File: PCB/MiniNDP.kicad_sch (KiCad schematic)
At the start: 20 parts, among them J1 Conn_02x20_Odd_Even, U1 HC161, U2 HC161, U3 HC161, U4 HC138, U5 HC574, U6 AS6C4008, U7 1G32, U8 1G79

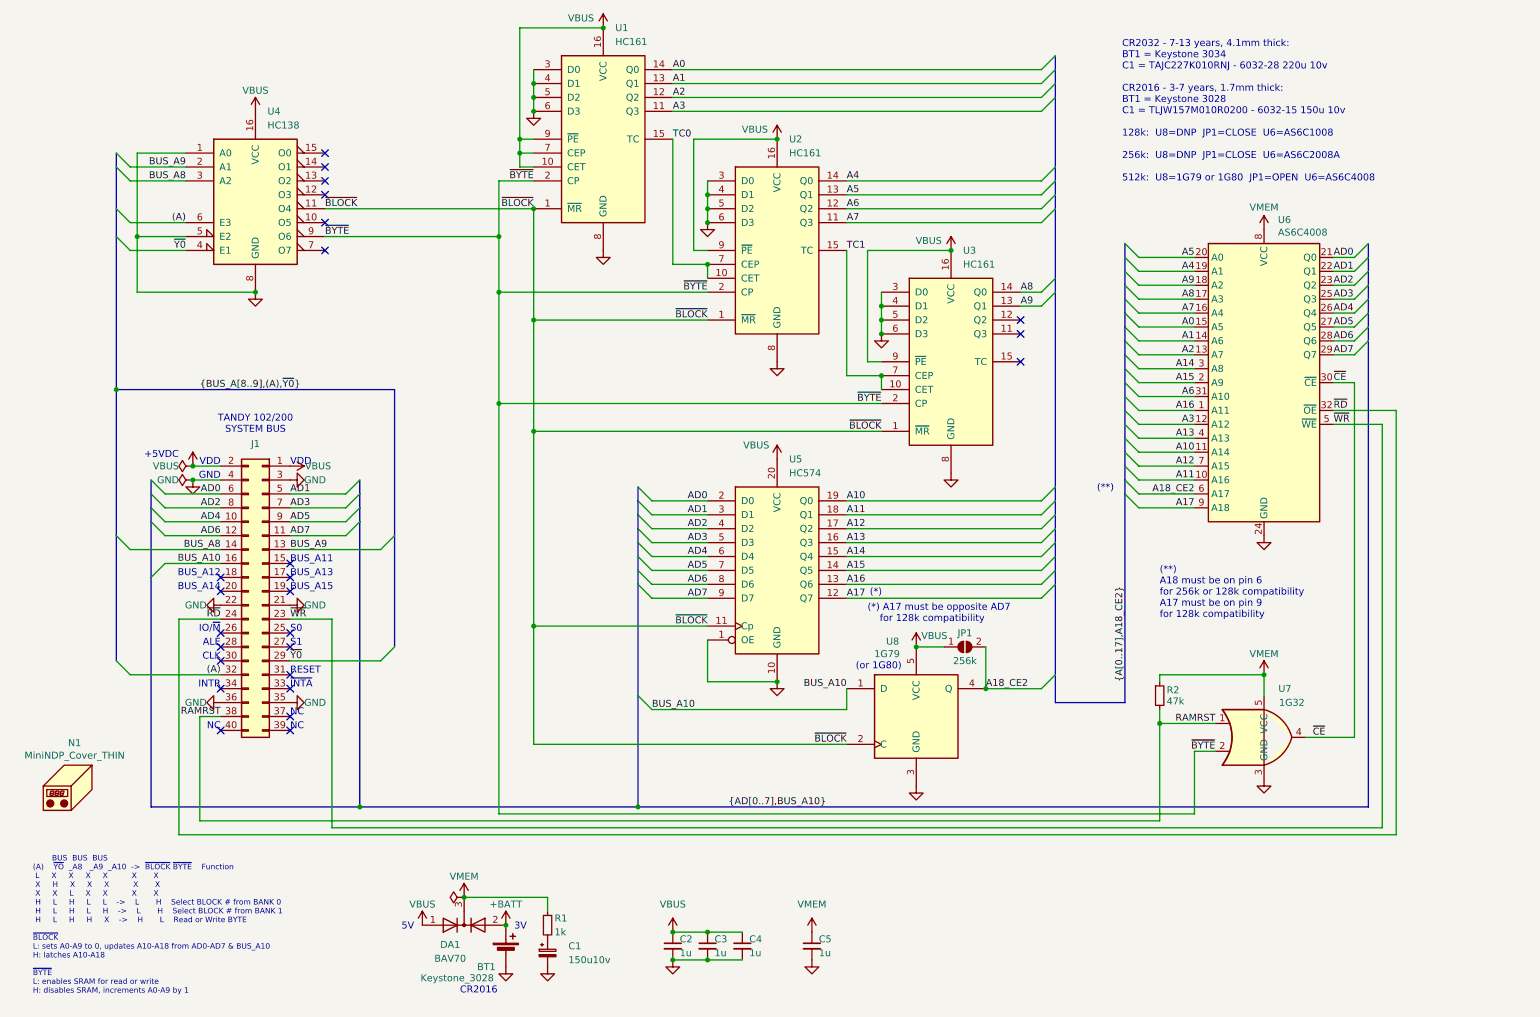
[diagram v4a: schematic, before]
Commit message: make EZ1M the default
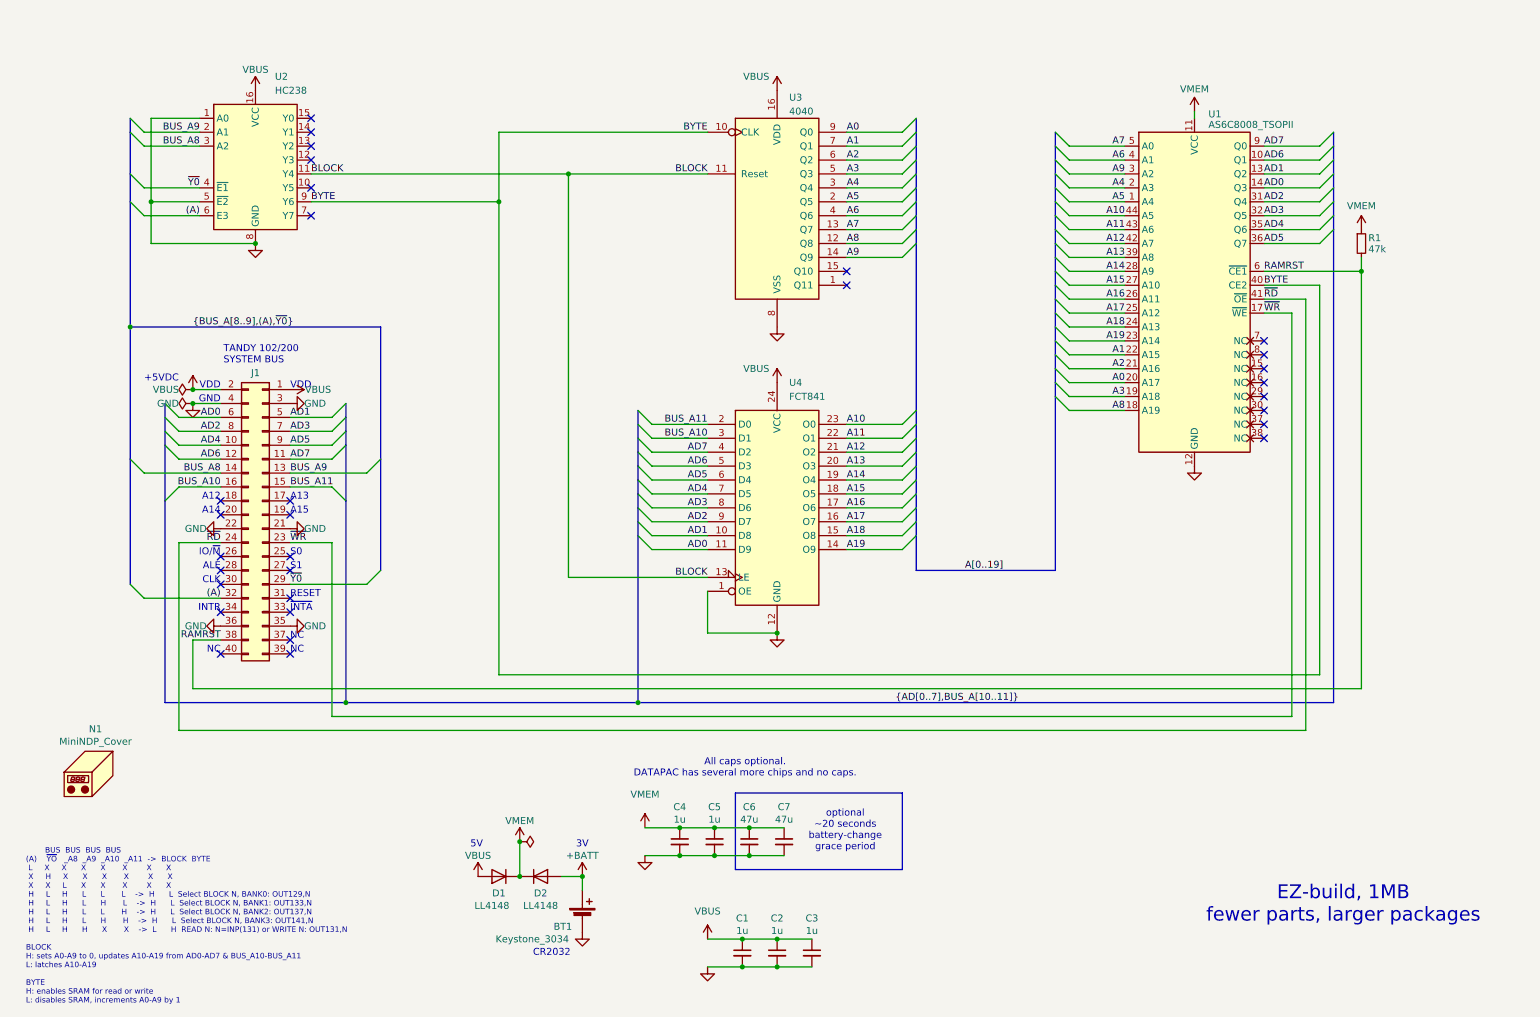
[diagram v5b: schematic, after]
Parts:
- removed C1: 150u10v, 000_LOCAL:CP_6032, symbol 000_LOCAL:C_Polarized
- removed DA1: BAV70, 000_LOCAL:SOT-23, symbol 000_LOCAL:BAV70
- removed JP1: 256k, 000_LOCAL:SolderJumper-2_Open 0.65mm, symbol 000_LOCAL:SolderJumper_2_Open
- removed R1: 1k, 000_LOCAL:R_0805, symbol 000_LOCAL:R
- removed U1, U2, U3: HC161, 000_LOCAL:TSSOP-16, symbol 000_LOCAL:74xx161
- removed U4: HC138, 000_LOCAL:TSSOP-16, symbol 000_LOCAL:74xx138
- removed U5: HC574, 000_LOCAL:TSSOP-20, symbol 000_LOCAL:74xx574
- removed U7: 1G32, 000_LOCAL:SOT-353_SC-70-5, symbol 000_LOCAL:74xx1G32
- removed U8: 1G79, 000_LOCAL:SOT-353_SC-70-5, symbol 000_LOCAL:74xx1G79
- added C1: 1u, 000_LOCAL:C_0805, symbol 000_LOCAL:C
- added C6, C7: 47u, 000_LOCAL:C_1206, symbol 000_LOCAL:C
- added D1, D2: LL4148, 000_LOCAL:D_MiniMELF, symbol 000_LOCAL:LL4148
- added U2: HC238, 000_LOCAL:SOIC-16_3.9x9.9mm_P1.27mm, symbol 000_LOCAL:HC238
- added U3: 4040, 000_LOCAL:SOIC-16_3.9x9.9mm_P1.27mm, symbol 000_LOCAL:4040
- added U4: FCT841, 000_LOCAL:SOIC-24, symbol 000_LOCAL:FCT841
- BT1: value Keystone_3028 -> Keystone_3034; MPN Keystone_3028 -> Keystone 3034
- N1: value MiniNDP_Cover_THIN -> MiniNDP_Cover; footprint 000_LOCAL:MiniNDP_Cover_THIN -> 000_LOCAL:MiniNDP_Cover; MPN MiniNDP_Cover_THIN.stl -> MiniNDP_Cover.stl
- U1: renamed from U6; value AS6C4008 -> AS6C8008_TSOPII; footprint 000_LOCAL:TSOP32-dual -> 000_LOCAL:TSOP-II-44; symbol 000_LOCAL:AS6C4008_TSOP -> 000_LOCAL:AS6C8008_TSOPII; MPN AS6C4008-55STIN -> AS6C8008-55ZIN
- renumbered R2 to R1
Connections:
- net A18_CE2 is gone; now on net RAMRST: U1.6 (~{CE1})
- net (A): now also U2.6 (E3)
- net +BATT: now also D2.2 (A)
- net A0: now also U1.20 (A17), U3.9 (Q0); no longer U1.15 (A5)
- net A1: now also U1.22 (A15), U3.7 (Q1); no longer U1.14 (A6)
- net A10: now also U1.44 (A5), U4.23 (O0); no longer U1.11 (A14)
- net A11: now also U1.43 (A6), U4.22 (O1); no longer U1.10 (A16)
- net A12: now also U1.42 (A7), U4.21 (O2); no longer U1.7 (A15)
- net A13: now also U1.39 (A8), U4.20 (O3); no longer U1.4 (A13)
- net A14: now also U1.28 (A9), U4.19 (O4); no longer U1.3 (A8)
- net A15: now also U1.27 (A10), U4.18 (O5); no longer U1.2 (A9)
- net A16: now also U1.26 (A11), U4.17 (O6); no longer U1.1 (A11)
- net A17: now also U1.25 (A12), U4.16 (O7); no longer U1.9 (A18)
- net A2: now also U1.21 (A16), U3.6 (Q2); no longer U1.13 (A7)
- net A3: now also U1.19 (A18), U3.5 (Q3); no longer U1.12 (A12)
- net A4: now also U1.2 (A3), U3.3 (Q4); no longer U1.19 (A1)
- net A5: now also U1.1 (A4), U3.2 (Q5); no longer U1.20 (A0)
- net A6: now also U1.4 (A1), U3.4 (Q6); no longer U1.31 (A10)
- net A7: now also U1.5 (A0), U3.13 (Q7); no longer U1.16 (A4)
- net A8: now also U1.18 (A19), U3.12 (Q8); no longer U1.17 (A3)
- net A9: now also U1.3 (A2), U3.14 (Q9); no longer U1.18 (A2)
- net AD0: now also U1.14 (Q3), U4.11 (D9); no longer U1.21 (Q0)
- net AD1: now also U1.13 (Q2), U4.10 (D8); no longer U1.22 (Q1)
- net AD2: now also U1.31 (Q4), U4.9 (D7); no longer U1.23 (Q2)
- net AD3: now also U1.32 (Q5), U4.8 (D6); no longer U1.25 (Q3)
- net AD4: now also U1.35 (Q6), U4.7 (D5); no longer U1.26 (Q4)
- net AD5: now also U1.36 (Q7), U4.6 (D4); no longer U1.27 (Q5)
- net AD6: now also U1.10 (Q1), U4.5 (D3); no longer U1.28 (Q6)
- net AD7: now also U1.9 (Q0), U4.4 (D2); no longer U1.29 (Q7)
- net BUS_A10: now also U4.3 (D1)
- net BUS_A8: now also U2.3 (A2)
- net BUS_A9: now also U2.2 (A1)
- net GND: now also U1.12 (GND), U1.34 (GND), C1.2, C6.2, C7.2, U2.1 (A0), U2.5 (~{E2}), U2.8 (GND), U3.8 (VSS), U4.1 (OE), U4.12 (GND); no longer U1.24 (GND)
- net VBUS: now also C1.1, D1.2 (A), U2.16 (VCC), U3.16 (VDD), U4.24 (VCC); no longer C4.1
- net VMEM: now also C4.1, U1.11 (VCC), U1.33 (VCC), C6.1, C7.1, D1.1 (K), D2.1 (K); no longer U1.8 (VCC)
- net ~{RD}: now also U1.41 (~{OE}); no longer U1.32 (~{OE})
- net ~{WR}: now also U1.17 (~{WE}); no longer U1.5 (~{WE})
- net ~{Y0}: now also U2.4 (~{E1})
- net BUS_A11: now reaches J1.15 (Pin_15)
- net BUS_A11: now also U4.2 (D0)
- net ~{CE}: no longer names the net of U1.30 (NC)
- new net A18: U1.24 (A13), U4.15 (O8)
- new net A19: U1.23 (A14), U4.14 (O9)
- new net BLOCK: U2.11 (Y4), U3.11 (Reset), U4.13 (LE)
- new net BYTE: U1.40 (CE2), U2.9 (Y6), U3.10 (CLK)
- no-connect marks 25 -> 31
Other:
- note added: "A12"
- note added: "A13"
- note added: "A14"
- note added: "A15"
- note added: "All caps optional. DATAPAC has several more chips and no caps."
- note added: "BUS BUS BUS BUS (A) ~{YO} _A8 _A9 _A10 _A11 -> BLOCK BYTE L X X X X X X X X H X X X X X X X X L X X X X X H L H L L L -> H L Select BLOCK N, BANK0: OUT129,N H L H L H L -> H L Select BLOCK N, BANK1: OUT133,N H L H L L H -> H L Select BLOCK N, BANK2: OUT137,N H L H L H H -> H L Select BLOCK N, BANK3: OUT141,N H L H H X X -> L H READ N: N=INP(131) or WRITE N: OUT131,N BLOCK H: sets A0-A9 to 0, upda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"
- note added: "CR2032"
- note added: "EZ-build, 1MB fewer parts, larger packages"
- note added: "optional ~20 seconds battery-change grace period"
- note removed: "(*)"
- note removed: "(*) A17 must be opposite AD7 for 128k compatibility"
- note removed: "(**)"
- note removed: "(**) A18 must be on pin 6 for 256k or 128k compatibility A17 must be on pin 9 for 128k compatibility"
- note removed: "(or 1G80)"
- note removed: "BUS BUS BUS (A) ~{YO} _A8 _A9 _A10 -> ~{BLOCK} ~{BYTE} Function L X X X X X X X H X X X X X X X L X X X X H L H L L -> L H Select BLOCK # from BANK 0 H L H L H -> L H Select BLOCK # from BANK 1 H L H H X -> H L Read or Write BYTE ~{BLOCK} L: sets A0-A9 to 0, updates A10-A18 from AD0-AD7 & BUS_A10 H: latches A10-A18 ~{BYTE} L: enables SRAM for read or write H: disables SRAM, increments A0-A9 by 1"
- note removed: "BUS_A11"
- note removed: "BUS_A12"
- note removed: "BUS_A13"
- note removed: "BUS_A14"
- note removed: "BUS_A15"
- note removed: "CR2016"
- note removed: "CR2032 - 7-13 years, 4.1mm thick: BT1 = Keystone 3034 C1 = TAJC227K010RNJ - 6032-28 220u 10v CR2016 - 3-7 years, 1.7mm thick: BT1 = Keystone 3028 C1 = TLJW157M010R0200 - 6032-15 150u 10v 128k: U8=DNP JP1=CLOSE U6=AS6C1008 256k: U8=DNP JP1=CLOSE U6=AS6C2008A 512k: U8=1G79 or 1G80 JP1=OPEN U6=AS6C4008"
- moved on the sheet: BT1, J1, R1

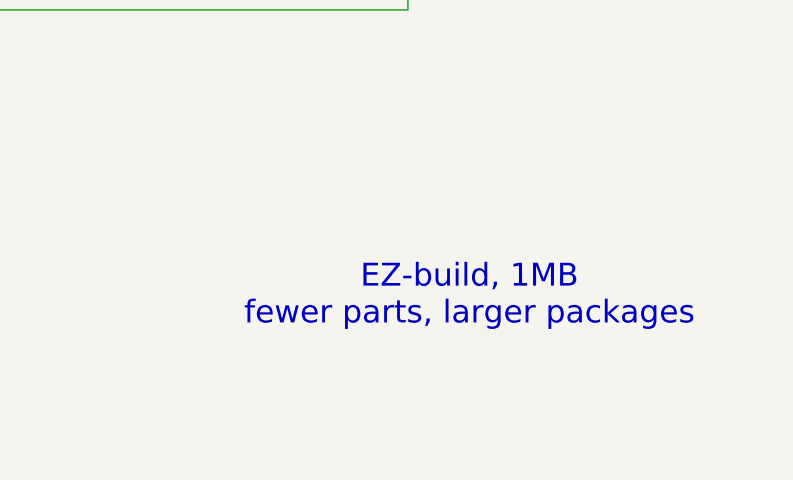
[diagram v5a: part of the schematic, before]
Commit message: ez1m rear silkscreen programming reference
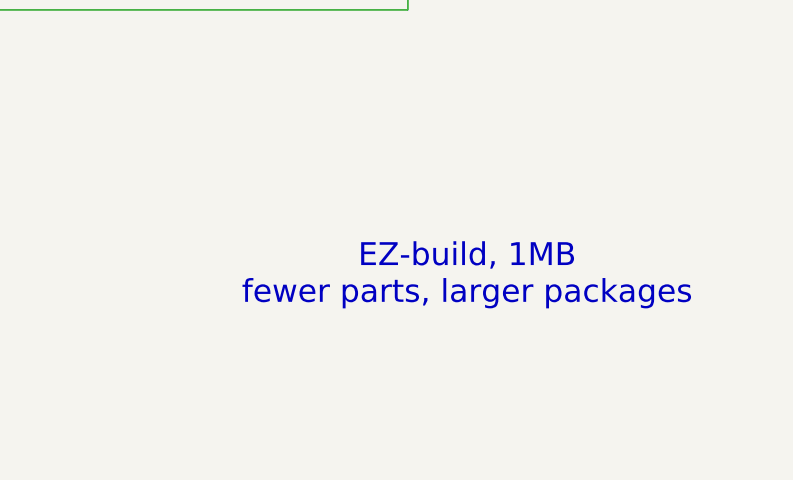
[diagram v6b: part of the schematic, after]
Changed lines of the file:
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@@
 	(text "EZ-build, 1MB\nfewer parts, larger packages"
 		(exclude_from_sim no)
-		(at 255.778 176.53 0)
+		(at 255.524 174.244 0)
 		(effects
 			(font

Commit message: silkscreen & pics
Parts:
- U3: value 4040 -> HC4040
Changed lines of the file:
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@@
 			)
 		)
-		(property "Value" "4040"
+		(property "Value" "HC4040"
 			(at 154.5941 31.75 0)
 			(effects

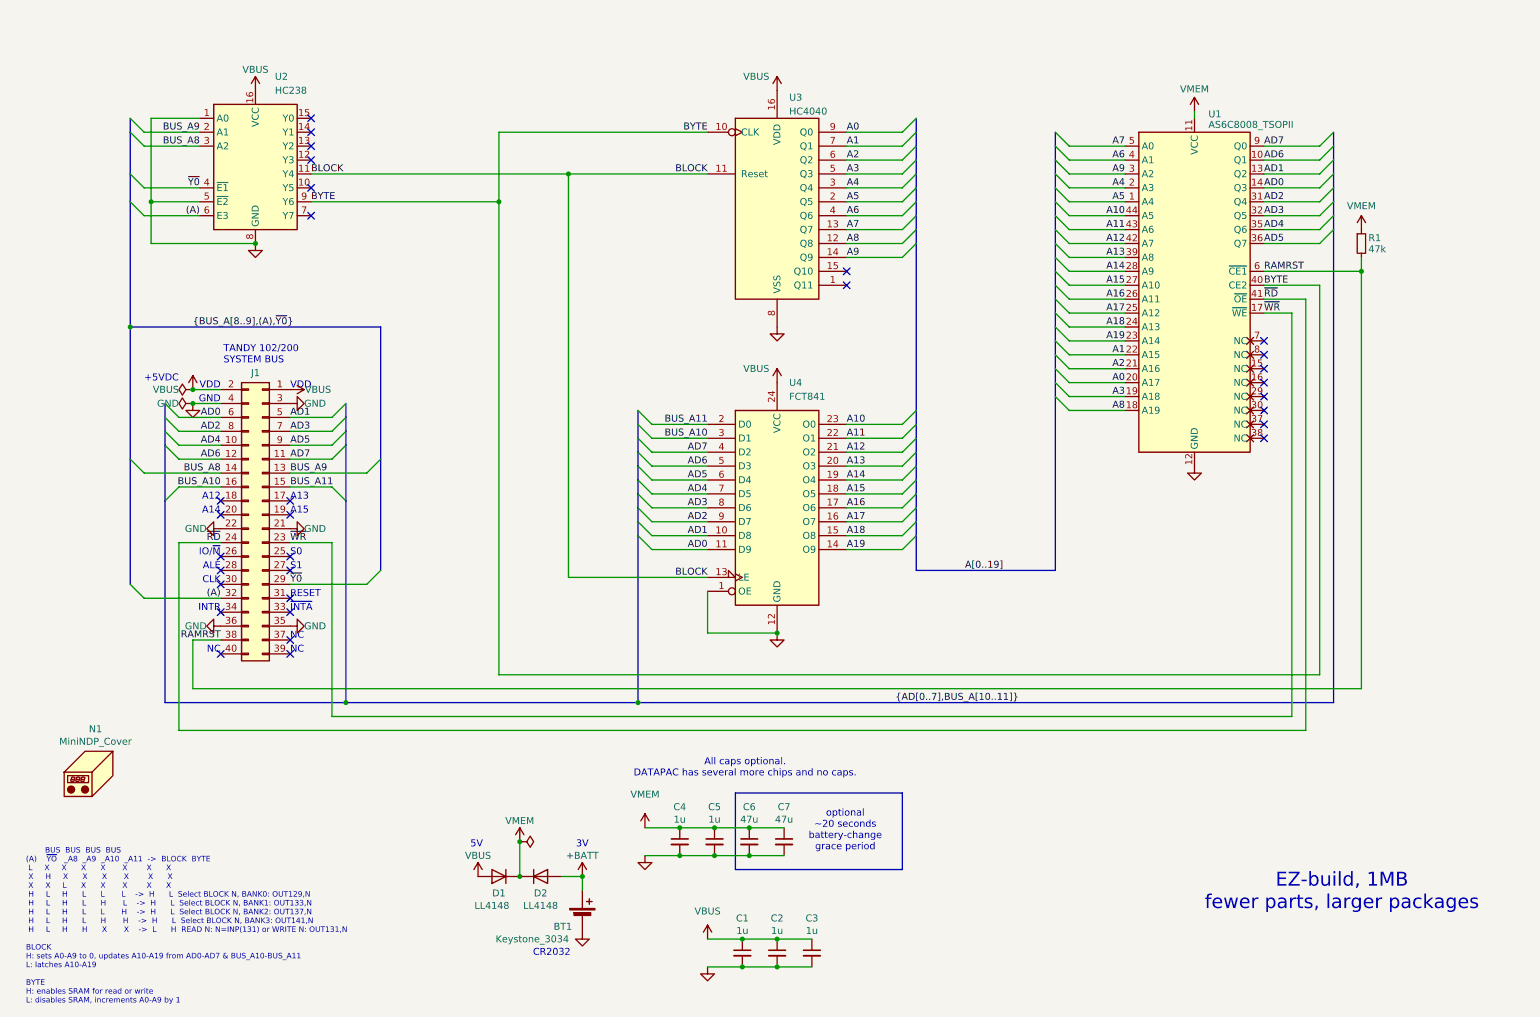
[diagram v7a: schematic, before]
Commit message: embed code font in pcb, bom export filename variables, delete extra battery trace
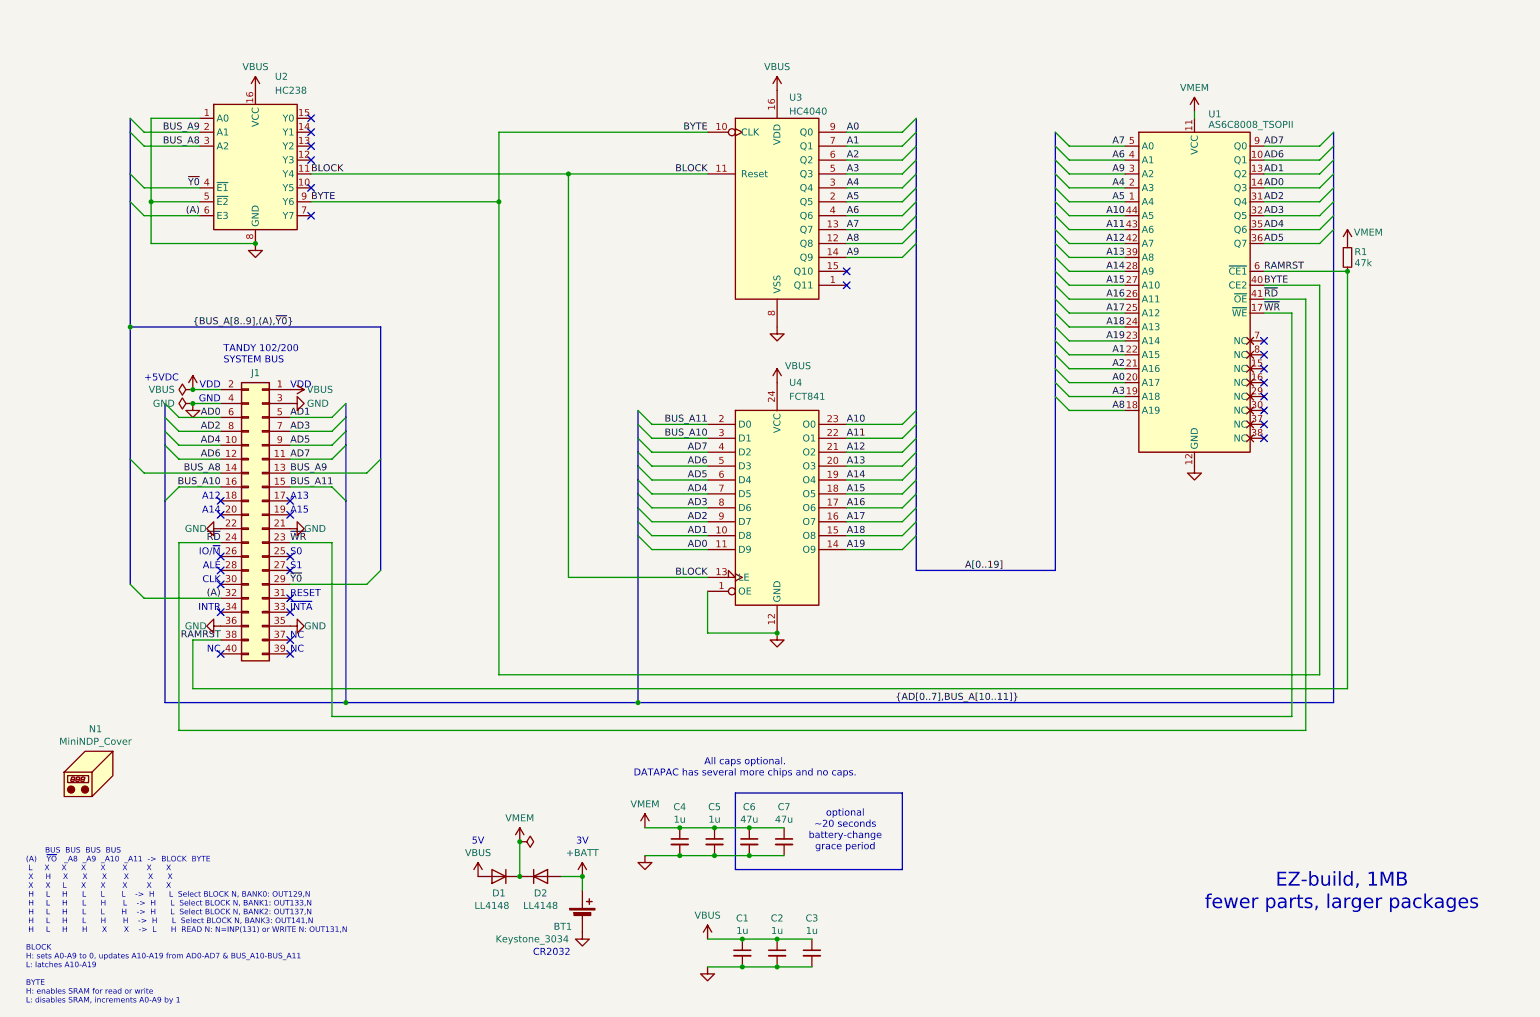
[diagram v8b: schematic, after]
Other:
- moved on the sheet: R1
